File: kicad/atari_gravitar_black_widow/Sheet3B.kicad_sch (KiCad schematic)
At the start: 107 parts, among them Q1 2N3904, Y1 12.096 MHZ

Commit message: more cap placements
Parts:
- C109, C126: footprint (none) -> Star_Wars_Vector_PCB:GenericComp
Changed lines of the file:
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@@
       (effects (font (size 1.27 1.27)) (justify left))
     )
-    (property "Footprint" "" (id 2) (at 89.8652 181.61 0)
+    (property "Footprint" "Star_Wars_Vector_PCB:GenericComp" (id 2) (at 89.8652 181.61 0)
       (effects (font (size 1.27 1.27)) hide)
     )
@@
       (effects (font (size 1.27 1.27)) (justify left))
     )
-    (property "Footprint" "" (id 2) (at 101.9302 275.59 0)
-      (effects (font (size 1.27 1.27)) hide)
-    )
+    (property "Footprint" "Star_Wars_Vector_PCB:GenericComp" (id 2) (at 101.9302 275.59 0)
+      (effects (font (size 1.27 1.27)) hide)
+    )

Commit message: more cap placements
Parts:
- C48: footprint Star_Wars_Vector_PCB:GenericComp -> Star_Wars_Vector_PCB:CapBrown
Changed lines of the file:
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@@
       (effects (font (size 1.27 1.27)) (justify left))
     )
-    (property "Footprint" "Star_Wars_Vector_PCB:GenericComp" (id 2) (at 149.5552 242.57 0)
+    (property "Footprint" "Star_Wars_Vector_PCB:CapBrown" (id 2) (at 149.5552 242.57 0)
       (effects (font (size 1.27 1.27)) hide)
     )

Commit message: caps placement up to c126
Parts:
- C117, C119, C120: footprint (none) -> Star_Wars_Vector_PCB:LargeCap
- C121: footprint (none) -> Star_Wars_Vector_PCB:CapElec2
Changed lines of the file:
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@@
       (effects (font (size 1.27 1.27)) (justify left))
     )
-    (property "Footprint" "" (id 2) (at 111.76 150.495 0)
+    (property "Footprint" "Star_Wars_Vector_PCB:CapElec2" (id 2) (at 111.76 150.495 0)
       (effects (font (size 1.27 1.27)) hide)
     )
@@
       (effects (font (size 1.27 1.27)) (justify right))
     )
-    (property "Footprint" "" (id 2) (at 74.295 128.27 0)
+    (property "Footprint" "Star_Wars_Vector_PCB:LargeCap" (id 2) (at 74.295 128.27 0)
       (effects (font (size 1.27 1.27)) hide)
     )
@@
       (effects (font (size 1.27 1.27)) (justify left))
     )
-    (property "Footprint" "" (id 2) (at 74.295 150.495 0)
+    (property "Footprint" "Star_Wars_Vector_PCB:LargeCap" (id 2) (at 74.295 150.495 0)
       (effects (font (size 1.27 1.27)) hide)
     )
@@
       (effects (font (size 1.27 1.27)) (justify left))
     )
-    (property "Footprint" "" (id 2) (at 74.295 210.82 0)
+    (property "Footprint" "Star_Wars_Vector_PCB:LargeCap" (id 2) (at 74.295 210.82 0)
       (effects (font (size 1.27 1.27)) hide)
     )

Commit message: resistor placements R1-R153
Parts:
- R107, R22, R23, R40, R41, R42, R55, R69, R70, R71, R72, R73, R82: footprint (none) -> Star_Wars_Vector_PCB:GenericComp
- Y1: footprint (none) -> Star_Wars_Main_PCB:Y
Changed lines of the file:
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@@
       (effects (font (size 1.27 1.27)) (justify left))
     )
-    (property "Footprint" "" (id 2) (at 77.851 197.739 90)
+    (property "Footprint" "Star_Wars_Vector_PCB:GenericComp" (id 2) (at 77.851 197.739 90)
       (effects (font (size 1.27 1.27)) hide)
     )
@@
       (effects (font (size 1.27 1.27)) (justify left))
     )
-    (property "Footprint" "" (id 2) (at 84.836 197.739 90)
+    (property "Footprint" "Star_Wars_Vector_PCB:GenericComp" (id 2) (at 84.836 197.739 90)
       (effects (font (size 1.27 1.27)) hide)
     )
@@
       (effects (font (size 1.27 1.27)) (justify left))
     )
-    (property "Footprint" "" (id 2) (at 91.821 197.739 90)
+    (property "Footprint" "Star_Wars_Vector_PCB:GenericComp" (id 2) (at 91.821 197.739 90)
       (effects (font (size 1.27 1.27)) hide)
     )
@@
       (effects (font (size 1.27 1.27)) (justify left))
     )
-    (property "Footprint" "" (id 2) (at 93.726 206.629 90)
+    (property "Footprint" "Star_Wars_Vector_PCB:GenericComp" (id 2) (at 93.726 206.629 90)
       (effects (font (size 1.27 1.27)) hide)
     )
@@
       (effects (font (size 1.27 1.27)) (justify left))
     )
-    (property "Footprint" "" (id 2) (at 242.316 136.144 90)
+    (property "Footprint" "Star_Wars_Vector_PCB:GenericComp" (id 2) (at 242.316 136.144 90)
       (effects (font (size 1.27 1.27)) hide)
     )
@@
       (effects (font (size 1.27 1.27)) (justify left))
     )
-    (property "Footprint" "" (id 2) (at 242.316 156.464 90)
+    (property "Footprint" "Star_Wars_Vector_PCB:GenericComp" (id 2) (at 242.316 156.464 90)
       (effects (font (size 1.27 1.27)) hide)
     )
@@
       (effects (font (size 1.27 1.27)) (justify left))
     )
-    (property "Footprint" "" (id 2) (at 258.445 156.21 0)
+    (property "Footprint" "Star_Wars_Main_PCB:Y" (id 2) (at 258.445 156.21 0)
       (effects (font (size 1.27 1.27)) hide)
     )
@@
       (effects (font (size 1.27 1.27)) (justify left))
     )
-    (property "Footprint" "" (id 2) (at 307.721 171.704 90)
+    (property "Footprint" "Star_Wars_Vector_PCB:GenericComp" (id 2) (at 307.721 171.704 90)
       (effects (font (size 1.27 1.27)) hide)
     )
@@
       (effects (font (size 1.27 1.27)) (justify left))
     )
-    (property "Footprint" "" (id 2) (at 259.461 196.469 90)
+    (property "Footprint" "Star_Wars_Vector_PCB:GenericComp" (id 2) (at 259.461 196.469 90)
       (effects (font (size 1.27 1.27)) hide)
     )
@@
       (effects (font (size 1.27 1.27)) (justify left))
     )
-    (property "Footprint" "" (id 2) (at 277.241 204.851 90)
+    (property "Footprint" "Star_Wars_Vector_PCB:GenericComp" (id 2) (at 277.241 204.851 90)
       (effects (font (size 1.27 1.27)) hide)
     )
@@
       (effects (font (size 1.27 1.27)) (justify left))
     )
-    (property "Footprint" "" (id 2) (at 300.101 204.851 90)
+    (property "Footprint" "Star_Wars_Vector_PCB:GenericComp" (id 2) (at 300.101 204.851 90)
       (effects (font (size 1.27 1.27)) hide)
     )
@@
       (effects (font (size 1.27 1.27)) (justify left))
     )
-    (property "Footprint" "" (id 2) (at 249.936 217.551 90)
+    (property "Footprint" "Star_Wars_Vector_PCB:GenericComp" (id 2) (at 249.936 217.551 90)
       (effects (font (size 1.27 1.27)) hide)
     )
@@
       (effects (font (size 1.27 1.27)) (justify left))
     )
-    (property "Footprint" "" (id 2) (at 292.481 232.029 90)
+    (property "Footprint" "Star_Wars_Vector_PCB:GenericComp" (id 2) (at 292.481 232.029 90)
       (effects (font (size 1.27 1.27)) hide)
     )
@@
       (effects (font (size 1.27 1.27)) (justify left))
     )
-    (property "Footprint" "" (id 2) (at 418.211 223.139 90)
-      (effects (font (size 1.27 1.27)) hide)
-    )
+    (property "Footprint" "Star_Wars_Vector_PCB:GenericComp" (id 2) (at 418.211 223.139 90)
+      (effects (font (size 1.27 1.27)) hide)
+    )

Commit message: all resistors placed.
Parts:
- R195: footprint (none) -> Star_Wars_Vector_PCB:Inductor1
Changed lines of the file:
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@@
       (effects (font (size 1.27 1.27)) (justify left))
     )
-    (property "Footprint" "" (id 2) (at 75.311 168.529 90)
+    (property "Footprint" "Star_Wars_Vector_PCB:Inductor1" (id 2) (at 75.311 168.529 90)
       (effects (font (size 1.27 1.27)) hide)
     )

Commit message: ALL PARTS PLACED!!
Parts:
- C110, C111: footprint (none) -> Star_Wars_Vector_PCB:CapElec2
- CR3, CR5, CR7, CR8: footprint (none) -> quantum_arcade_pcb:Diode
- CR6: footprint (none) -> Star_Wars_Vector_PCB:LED
- L1: footprint (none) -> Star_Wars_Vector_PCB:Inductor1
- Q1: footprint (none) -> quantum_arcade_pcb:GenTrans
- VR1, VR2: footprint (none) -> quantum_arcade_pcb:BigTrans
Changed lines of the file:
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@@
     (property "Reference" "VR1" (id 0) (at 111.125 115.7732 0))
     (property "Value" "7915" (id 1) (at 111.125 118.0846 0))
-    (property "Footprint" "" (id 2) (at 111.125 121.92 0)
+    (property "Footprint" "quantum_arcade_pcb:BigTrans" (id 2) (at 111.125 121.92 0)
       (effects (font (size 5.08 5.08)) hide)
     )
@@
       (effects (font (size 1.27 1.27)) (justify right))
     )
-    (property "Footprint" "" (id 2) (at 139.065 128.27 0)
+    (property "Footprint" "quantum_arcade_pcb:Diode" (id 2) (at 139.065 128.27 0)
       (effects (font (size 1.27 1.27)) hide)
     )
@@
       (effects (font (size 1.27 1.27)) (justify left))
     )
-    (property "Footprint" "" (id 2) (at 127 150.495 0)
+    (property "Footprint" "quantum_arcade_pcb:Diode" (id 2) (at 127 150.495 0)
       (effects (font (size 1.27 1.27)) hide)
     )
@@
     (property "Reference" "VR2" (id 0) (at 99.06 137.9982 0))
     (property "Value" "7815" (id 1) (at 99.06 140.3096 0))
-    (property "Footprint" "" (id 2) (at 99.06 144.145 0)
+    (property "Footprint" "quantum_arcade_pcb:BigTrans" (id 2) (at 99.06 144.145 0)
       (effects (font (size 5.08 5.08)) hide)
     )
@@
       (effects (font (size 1.27 1.27)) (justify left))
     )
-    (property "Footprint" "" (id 2) (at 74.295 177.8 0)
+    (property "Footprint" "quantum_arcade_pcb:Diode" (id 2) (at 74.295 177.8 0)
       (effects (font (size 1.27 1.27)) hide)
     )
@@
       (effects (font (size 1.27 1.27)) (justify right))
     )
-    (property "Footprint" "" (id 2) (at 92.71 215.265 0)
+    (property "Footprint" "Star_Wars_Vector_PCB:LED" (id 2) (at 92.71 215.265 0)
       (effects (font (size 1.27 1.27)) hide)
     )
@@
       (effects (font (size 1.27 1.27)) (justify left))
     )
-    (property "Footprint" "" (id 2) (at 306.705 161.925 0)
+    (property "Footprint" "Star_Wars_Vector_PCB:Inductor1" (id 2) (at 306.705 161.925 0)
       (effects (font (size 1.27 1.27)) hide)
     )
@@
       (effects (font (size 1.27 1.27)) (justify left))
     )
-    (property "Footprint" "" (id 2) (at 309.245 147.955 0)
+    (property "Footprint" "quantum_arcade_pcb:GenTrans" (id 2) (at 309.245 147.955 0)
       (effects (font (size 1.27 1.27) italic) (justify left) hide)
     )
@@
       (effects (font (size 1.27 1.27)) (justify left))
     )
-    (property "Footprint" "" (id 2) (at 314.325 233.68 0)
+    (property "Footprint" "quantum_arcade_pcb:Diode" (id 2) (at 314.325 233.68 0)
       (effects (font (size 1.27 1.27)) hide)
     )
@@
       (effects (font (size 1.27 1.27)) (justify right))
     )
-    (property "Footprint" "" (id 2) (at 91.44 128.27 0)
+    (property "Footprint" "Star_Wars_Vector_PCB:CapElec2" (id 2) (at 91.44 128.27 0)
       (effects (font (size 1.27 1.27)) hide)
     )
@@
       (effects (font (size 1.27 1.27)) (justify right))
     )
-    (property "Footprint" "" (id 2) (at 123.825 128.27 0)
-      (effects (font (size 1.27 1.27)) hide)
-    )
+    (property "Footprint" "Star_Wars_Vector_PCB:CapElec2" (id 2) (at 123.825 128.27 0)
+      (effects (font (size 1.27 1.27)) hide)
+    )

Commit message: ROW 7 TOPSIDE TRACES COMPLETED
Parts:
- C48: footprint Star_Wars_Vector_PCB:CapBrown -> Star_Wars_Vector_PCB:GenericComp
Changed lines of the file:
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@@
       (effects (font (size 1.27 1.27)) (justify left))
     )
-    (property "Footprint" "Star_Wars_Vector_PCB:CapBrown" (id 2) (at 149.5552 242.57 0)
+    (property "Footprint" "Star_Wars_Vector_PCB:GenericComp" (id 2) (at 149.5552 242.57 0)
       (effects (font (size 1.27 1.27)) hide)
     )

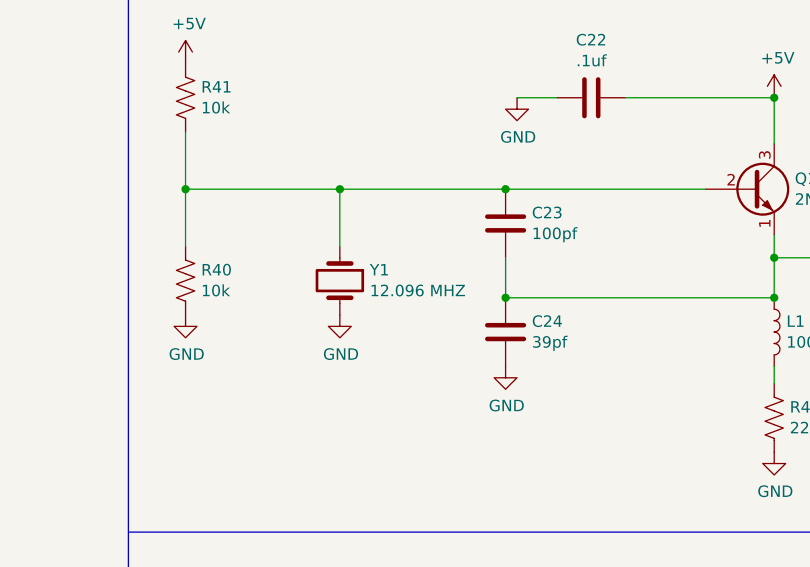
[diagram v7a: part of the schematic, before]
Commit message: Fixed all schematic warnings and fixed the edge cuts
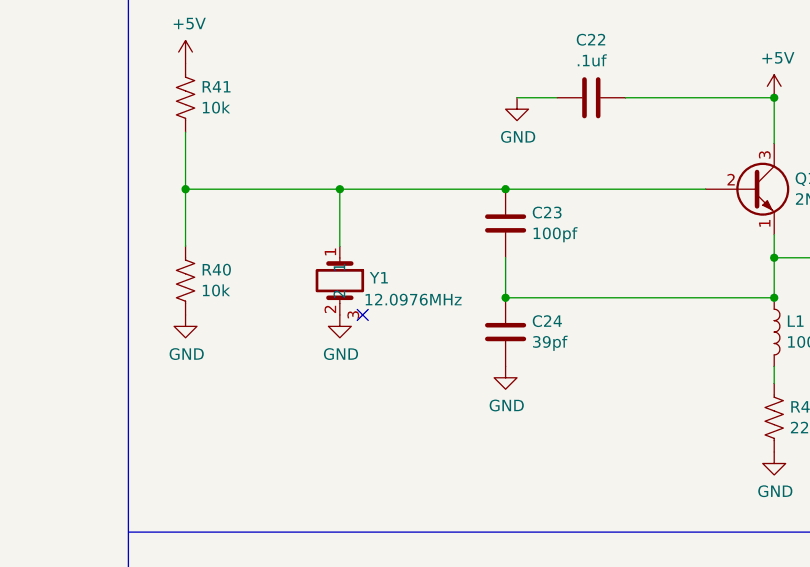
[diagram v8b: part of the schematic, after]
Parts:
- removed Y1: 12.096 MHZ, Star_Wars_Main_PCB:Y, symbol Device:Crystal
- added Y1: 12.0976MHz, Star_Wars_Main_PCB:Y, symbol atari_grav_bw:Crystal
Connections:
- net GND: now also Y1.2
- net at C23.1, Q1.2 (B), R40.1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: now also Y1.1
- no-connect marks 14 -> 15
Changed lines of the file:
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@@
   (junction (at 72.39 266.7) (diameter 0) (color 0 0 0 0)
   )
+  (no_connect (at 260.985 160.02))
   (no_connect (at 485.14 261.62))
   (no_connect (at 442.595 274.32))
@@
     (pin "2")
   )
-  (symbol (lib_id "Device:Crystal") (at 258.445 156.21 270) (unit 1)
-    (in_bom yes) (on_board yes)
-    (property "Reference" "Y1" (id 0) (at 261.7724 155.0416 90)
-      (effects (font (size 1.27 1.27)) (justify left))
-    )
-    (property "Value" "12.096 MHZ" (id 1) (at 261.7724 157.353 90)
-      (effects (font (size 1.27 1.27)) (justify left))
-    )
-    (property "Footprint" "Star_Wars_Main_PCB:Y" (id 2) (at 258.445 156.21 0)
-      (effects (font (size 1.27 1.27)) hide)
-    )
-    (property "Datasheet" "~" (id 3) (at 258.445 156.21 0)
-      (effects (font (size 1.27 1.27)) hide)
-    )
-    (pin "1")
-    (pin "2")
-  )
   (symbol (lib_id "Device:C") (at 276.86 149.86 0) (unit 1)
     (in_bom yes) (on_board yes)
@@
     (pin "1")
   )
+  (symbol (lib_id "atari_grav_bw:Crystal") (at 258.445 156.21 270) (unit 1)
+    (in_bom yes) (on_board yes)
+    (property "Reference" "Y1" (id 0) (at 261.7724 155.9365 90)
+      (effects (font (size 1.27 1.27)) (justify left))
+    )
+    (property "Value" "12.0976MHz" (id 1) (at 261.112 158.369 90)
+      (effects (font (size 1.27 1.27)) (justify left))
+    )
+    (property "Footprint" "Star_Wars_Main_PCB:Y" (id 2) (at 258.445 156.21 0)
+      (effects (font (size 1.27 1.27)) hide)
+    )
+    (property "Datasheet" "" (id 3) (at 258.445 156.21 0)
+      (effects (font (size 1.27 1.27)) hide)
+    )
+    (pin "1")
+    (pin "2")
+    (pin "3")
+  )
   (symbol (lib_id "Device:C_Polarized_US") (at 91.44 128.27 180) (unit 1)
